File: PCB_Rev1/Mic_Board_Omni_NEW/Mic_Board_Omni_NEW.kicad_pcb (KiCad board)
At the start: 2 copper layers, 51 x 31.5 mm, 34 parts, among them J2 532610771, J3 S2B-ZR-SM4A-TF_LF__SN_, U1 OPA1671IDBVR

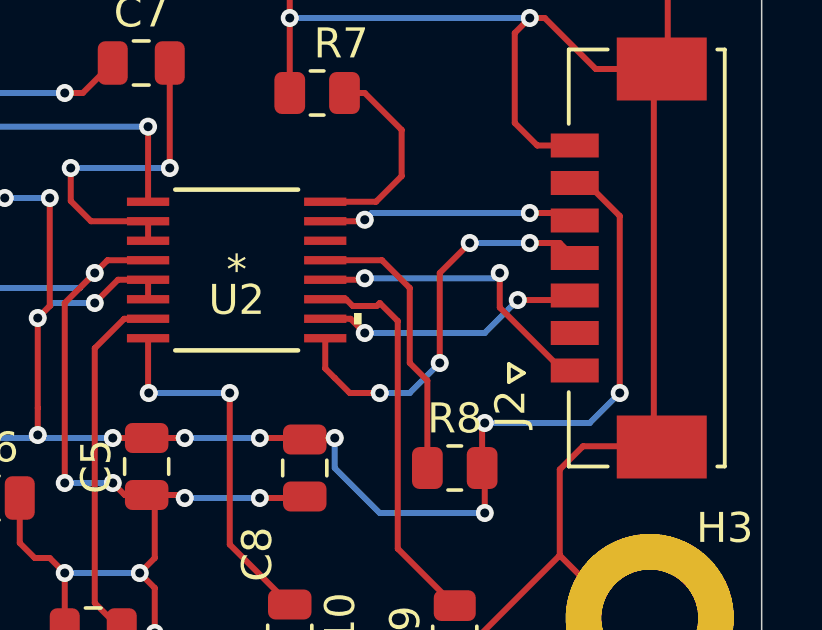
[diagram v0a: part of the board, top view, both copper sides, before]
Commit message: new mic boards added
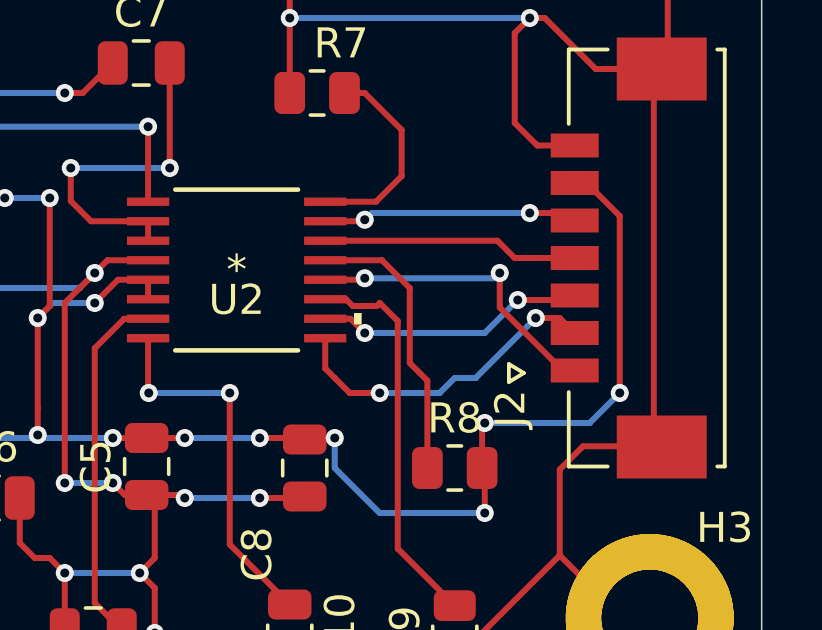
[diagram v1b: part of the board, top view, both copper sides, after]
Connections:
- J2 pad 2: unconnected-(J2-Pad2) -> Net-(U2-SDTO)
- J2 pad 4: Net-(U2-SDTO) -> Net-(U2-DIF/TDMI)
- U2 pad 14: unconnected-(U2-DIF/TDMI-Pad14) -> Net-(U2-DIF/TDMI)
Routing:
- net Net-(U2-DIF/TDMI): track 0.00 -> 8.56 mm
- net Net-(U2-SDTO): track 13.7 -> 10.9 mm, vias 4 -> 2
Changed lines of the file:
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@@
 	(net 16 "Net-(U2-LRCK)")
 	(net 17 "Net-(U2-BICK)")
-	(net 18 "unconnected-(J2-Pad2)")
+	(net 18 "Net-(U2-DIF{slash}TDMI)")
 	(net 19 "Net-(U2-FSEL)")
 	(net 20 "Net-(U2-PDN)")
-	(net 21 "unconnected-(U2-DIF{slash}TDMI-Pad14)")
 	(footprint "Footprints:ADC"
 		(layer "F.Cu")
@@
 		(property ki_fp_filters "SOIC_AK5720_AKM SOIC_AK5720_AKM-M SOIC_AK5720_AKM-L")
 		(sheetname "Root")
-		(sheetfile "Mic_Board_Unidirectional.kicad_sch")
+		(sheetfile "Mic_Board_Omni_NEW.kicad_sch")
 		(attr smd)
 		(fp_line
@@
 			(size 1.4097 0.2794)
 			(layers "F.Cu" "F.Paste" "F.Mask")
-			(net 21 "unconnected-(U2-DIF{slash}TDMI-Pad14)")
+			(net 18 "Net-(U2-DIF{slash}TDMI)")
 			(pinfunction "DIF/TDMI")
-			(pintype "unspecified+no_connect")
+			(pintype "unspecified")
 		)
 		(pad "15" smd rect
@@
 		(property ki_fp_filters "R_*")
 		(sheetname "Root")
-		(sheetfile "Mic_Board_Unidirectional.kicad_sch")
+		(sheetfile "Mic_Board_Omni_NEW.kicad_sch")
 		(attr smd)
 		(fp_line
@@
 		(property ki_fp_filters "C_*")
 		(sheetname "Root")
-		(sheetfile "Mic_Board_Unidirectional.kicad_sch")
+		(sheetfile "Mic_Board_Omni_NEW.kicad_sch")
 		(attr smd)
 		(fp_line
@@
 		(property ki_fp_filters "Pin* Test*")
 		(sheetname "Root")
-		(sheetfile "Mic_Board_Unidirectional.kicad_sch")
+		(sheetfile "Mic_Board_Omni_NEW.kicad_sch")
 		(attr exclude_from_pos_files)
 		(fp_circle
@@
 		)
 		(sheetname "Root")
-		(sheetfile "Mic_Board_Unidirectional.kicad_sch")
+		(sheetfile "Mic_Board_Omni_NEW.kicad_sch")
 		(attr smd)
 		(fp_line
@@
 		(property ki_fp_filters "R_*")
 		(sheetname "Root")
-		(sheetfile "Mic_Board_Unidirectional.kicad_sch")
+		(sheetfile "Mic_Board_Omni_NEW.kicad_sch")
 		(attr smd)
 		(fp_line
@@
 		(property ki_fp_filters "R_*")
 		(sheetname "Root")
-		(sheetfile "Mic_Board_Unidirectional.kicad_sch")
+		(sheetfile "Mic_Board_Omni_NEW.kicad_sch")
 		(attr smd)
 		(fp_line
@@
 		(property ki_fp_filters "SOT23-DBV5_TEX SOT23-DBV5_TEX-M SOT23-DBV5_TEX-L")
 		(sheetname "Root")
-		(sheetfile "Mic_Board_Unidirectional.kicad_sch")
+		(sheetfile "Mic_Board_Omni_NEW.kicad_sch")
 		(attr smd)
 		(fp_line
@@
 		(property ki_fp_filters "R_*")
 		(sheetname "Root")
-		(sheetfile "Mic_Board_Unidirectional.kicad_sch")
+		(sheetfile "Mic_Board_Omni_NEW.kicad_sch")
 		(attr smd)
 		(fp_line
@@
 		(property ki_fp_filters "C_*")
 		(sheetname "Root")
-		(sheetfile "Mic_Board_Unidirectional.kicad_sch")
+		(sheetfile "Mic_Board_Omni_NEW.kicad_sch")
 		(attr smd)
 		(fp_line
@@
 		(property ki_fp_filters "C_*")
 		(sheetname "Root")
-		(sheetfile "Mic_Board_Unidirectional.kicad_sch")
+		(sheetfile "Mic_Board_Omni_NEW.kicad_sch")
 		(attr smd)
 		(fp_line
@@
 		(property ki_fp_filters "R_*")
 		(sheetname "Root")
-		(sheetfile "Mic_Board_Unidirectional.kicad_sch")
+		(sheetfile "Mic_Board_Omni_NEW.kicad_sch")
 		(attr smd)
 		(fp_line
@@
 		(property ki_fp_filters "C_*")
 		(sheetname "Root")
-		(sheetfile "Mic_Board_Unidirectional.kicad_sch")
+		(sheetfile "Mic_Board_Omni_NEW.kicad_sch")
 		(attr smd)
 		(fp_line
@@
 		(property ki_fp_filters "Pin* Test*")
 		(sheetname "Root")
-		(sheetfile "Mic_Board_Unidirectional.kicad_sch")
+		(sheetfile "Mic_Board_Omni_NEW.kicad_sch")
 		(attr exclude_from_pos_files)
 		(fp_circle
@@
 		(property ki_fp_filters "C_*")
 		(sheetname "Root")
-		(sheetfile "Mic_Board_Unidirectional.kicad_sch")
+		(sheetfile "Mic_Board_Omni_NEW.kicad_sch")
 		(attr smd)
 		(fp_line
@@
 		(property ki_fp_filters "C_*")
 		(sheetname "Root")
-		(sheetfile "Mic_Board_Unidirectional.kicad_sch")
+		(sheetfile "Mic_Board_Omni_NEW.kicad_sch")
 		(attr smd)
 		(fp_line
@@
 		(property ki_fp_filters "R_*")
 		(sheetname "Root")
-		(sheetfile "Mic_Board_Unidirectional.kicad_sch")
+		(sheetfile "Mic_Board_Omni_NEW.kicad_sch")
 		(attr smd)
 		(fp_line
@@
 		(property ki_fp_filters "R_*")
 		(sheetname "Root")
-		(sheetfile "Mic_Board_Unidirectional.kicad_sch")
+		(sheetfile "Mic_Board_Omni_NEW.kicad_sch")
 		(attr smd)
 		(fp_line
@@
 		(property ki_fp_filters "C_*")
 		(sheetname "Root")
-		(sheetfile "Mic_Board_Unidirectional.kicad_sch")
+		(sheetfile "Mic_Board_Omni_NEW.kicad_sch")
 		(attr smd)
 		(fp_line
@@
 		)
 		(sheetname "Root")
-		(sheetfile "Mic_Board_Unidirectional.kicad_sch")
+		(sheetfile "Mic_Board_Omni_NEW.kicad_sch")
 		(attr smd)
 		(fp_line
@@
 			(size 0.8 1.6)
 			(layers "F.Cu" "F.Paste")
-			(net 18 "unconnected-(J2-Pad2)")
+			(net 15 "Net-(U2-SDTO)")
 			(pinfunction "2")
-			(pintype "passive+no_connect")
+			(pintype "passive")
 		)
 		(pad "3" smd rect
@@
 			(size 0.8 1.6)
 			(layers "F.Cu" "F.Paste")
-			(net 15 "Net-(U2-SDTO)")
+			(net 18 "Net-(U2-DIF{slash}TDMI)")
 			(pinfunction "4")
 			(pintype "passive")
@@
 		(property ki_fp_filters "R_*")
 		(sheetname "Root")
-		(sheetfile "Mic_Board_Unidirectional.kicad_sch")
+		(sheetfile "Mic_Board_Omni_NEW.kicad_sch")
 		(attr smd)
 		(fp_line
@@
 		(property ki_fp_filters "C_*")
 		(sheetname "Root")
-		(sheetfile "Mic_Board_Unidirectional.kicad_sch")
+		(sheetfile "Mic_Board_Omni_NEW.kicad_sch")
 		(attr smd)
 		(fp_line
@@
 		(property ki_fp_filters "R_*")
 		(sheetname "Root")
-		(sheetfile "Mic_Board_Unidirectional.kicad_sch")
+		(sheetfile "Mic_Board_Omni_NEW.kicad_sch")
 		(attr smd)
 		(fp_line
@@
 		(property ki_fp_filters "C_*")
 		(sheetname "Root")
-		(sheetfile "Mic_Board_Unidirectional.kicad_sch")
+		(sheetfile "Mic_Board_Omni_NEW.kicad_sch")
 		(attr smd)
 		(fp_line
@@
 		(property ki_fp_filters "Pin* Test*")
 		(sheetname "Root")
-		(sheetfile "Mic_Board_Unidirectional.kicad_sch")
+		(sheetfile "Mic_Board_Omni_NEW.kicad_sch")
 		(attr exclude_from_pos_files)
 		(fp_circle
@@
 		(property ki_fp_filters "C_*")
 		(sheetname "Root")
-		(sheetfile "Mic_Board_Unidirectional.kicad_sch")
+		(sheetfile "Mic_Board_Omni_NEW.kicad_sch")
 		(attr smd)
 		(fp_line
@@
 		(property ki_fp_filters "C_*")
 		(sheetname "Root")
-		(sheetfile "Mic_Board_Unidirectional.kicad_sch")
+		(sheetfile "Mic_Board_Omni_NEW.kicad_sch")
 		(attr smd)
 		(fp_line
@@
 	)
 	(segment
-		(start 168.5 82)
-		(end 169.5 81)
-		(width 0.2)
-		(layer "F.Cu")
-		(net 15)
-	)
-	(segment
 		(start 164.68325 85.18325)
 		(end 165 85.5)
@@
 	)
 	(segment
-		(start 171.5 81)
-		(end 172.5 81)
-		(width 0.2)
-		(layer "F.Cu")
-		(net 15)
-	)
-	(segment
-		(start 168.5 85)
-		(end 168.5 82)
+		(start 172.500735 83.500735)
+		(end 173 84)
 		(width 0.2)
 		(layer "F.Cu")
@@
 	)
 	(segment
-		(start 172.5 81)
-		(end 173 81.5)
+		(start 171.699262 83.500735)
+		(end 172.500735 83.500735)
 		(width 0.2)
 		(layer "F.Cu")
@@
 	)
 	(via
-		(at 168.5 85)
+		(at 171.699262 83.500735)
 		(size 0.6)
 		(drill 0.3)
@@
 	)
 	(via
-		(at 169.5 81)
+		(at 166.5 86)
 		(size 0.6)
 		(drill 0.3)
@@
 		(net 15)
 	)
-	(via
-		(at 171.5 81)
-		(size 0.6)
-		(drill 0.3)
-		(layers "F.Cu" "B.Cu")
+	(segment
+		(start 167.5 86)
+		(end 168.5 86)
+		(width 0.2)
+		(layer "B.Cu")
 		(net 15)
 	)
-	(via
-		(at 166.5 86)
-		(size 0.6)
-		(drill 0.3)
-		(layers "F.Cu" "B.Cu")
+	(segment
+		(start 169 85.5)
+		(end 169.699997 85.5)
+		(width 0.2)
+		(layer "B.Cu")
 		(net 15)
 	)
 	(segment
-		(start 167.5 86)
-		(end 168.5 85)
+		(start 169.699997 85.5)
+		(end 171.699262 83.500735)
 		(width 0.2)
 		(layer "B.Cu")
@@
 	)
 	(segment
-		(start 169.5 81)
-		(end 171.5 81)
+		(start 168.5 86)
+		(end 169 85.5)
 		(width 0.2)
 		(layer "B.Cu")
@@
 	)
 	(segment
+		(start 173 81.5)
+		(end 171 81.5)
+		(width 0.2)
+		(layer "F.Cu")
+		(net 18)
+	)
+	(segment
+		(start 170.425003 80.925003)
+		(end 164.68325 80.925003)
+		(width 0.2)
+		(layer "F.Cu")
+		(net 18)
+	)
+	(segment
+		(start 164.688289 80.919964)
+		(end 164.68325 80.925003)
+		(width 0.2)
+		(layer "F.Cu")
+		(net 18)
+	)
+	(segment
+		(start 171 81.5)
+		(end 170.425003 80.925003)
+		(width 0.2)
+		(layer "F.Cu")
+		(net 18)
+	)
+	(segment
 		(start 165.949999 80.275004)
 		(end 166 80.225003)
@@
 		(net 20)
 	)
-	(segment
-		(start 164.688289 80.919964)
-		(end 164.68325 80.925003)
-		(width 0.2)
-		(layer "F.Cu")
-		(net 21)
-	)
 )

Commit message: MICBOARD OMNI CSV DONE
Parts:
- removed J3: S2B-ZR-SM4A-TF_LF__SN_, Footprints:Mic_Conn
- added MK1: Microphone, Footprints:Omnidirectional, F.Cu at (133.5, 80.5)
- moved R2 4.00 mm to (148.0, 70.0)
- moved C1 2.86 mm to (141.0, 73.5)
- moved R1 2.06 mm to (141.0, 70.0)
- moved R4 1.50 mm to (146.0, 75.0)
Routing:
- net Net-(C1-Pad1): track 21.9 -> 14.4 mm, vias 6 -> 2
- net GND: track 173.4 -> 169.4 mm, vias 16 -> 18
- net Net-(U1-+IN): track 31.1 -> 27.1 mm, vias 4 -> 2
- net +3V3: track 74.3 -> 71.9 mm
- net Net-(MK1-+): track 36.8 -> 38.4 mm, vias 3 -> 2
